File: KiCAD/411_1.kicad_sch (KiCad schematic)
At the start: 89 parts, among them J1 Conn_Coaxial, J2 Conn_Coaxial, J3 Conn_Coaxial, J4 Conn_01x05, SW1 SW_Push, U1 LM2937IMP, U2 MCP6L04x-xSL, U3 TMUX1101, U4 LA72914V-TLM-H, U5 ATtiny85V-10S

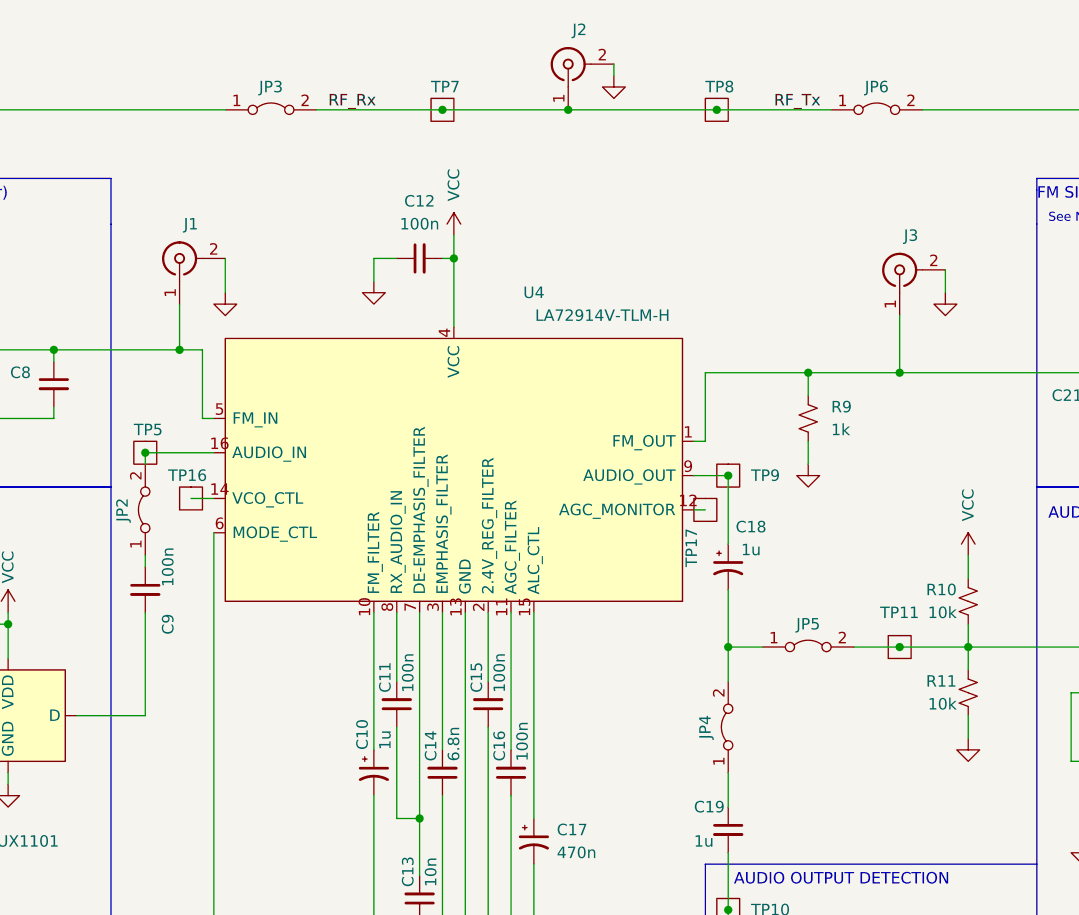
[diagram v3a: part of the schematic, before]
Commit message: Added info to components for bom generation
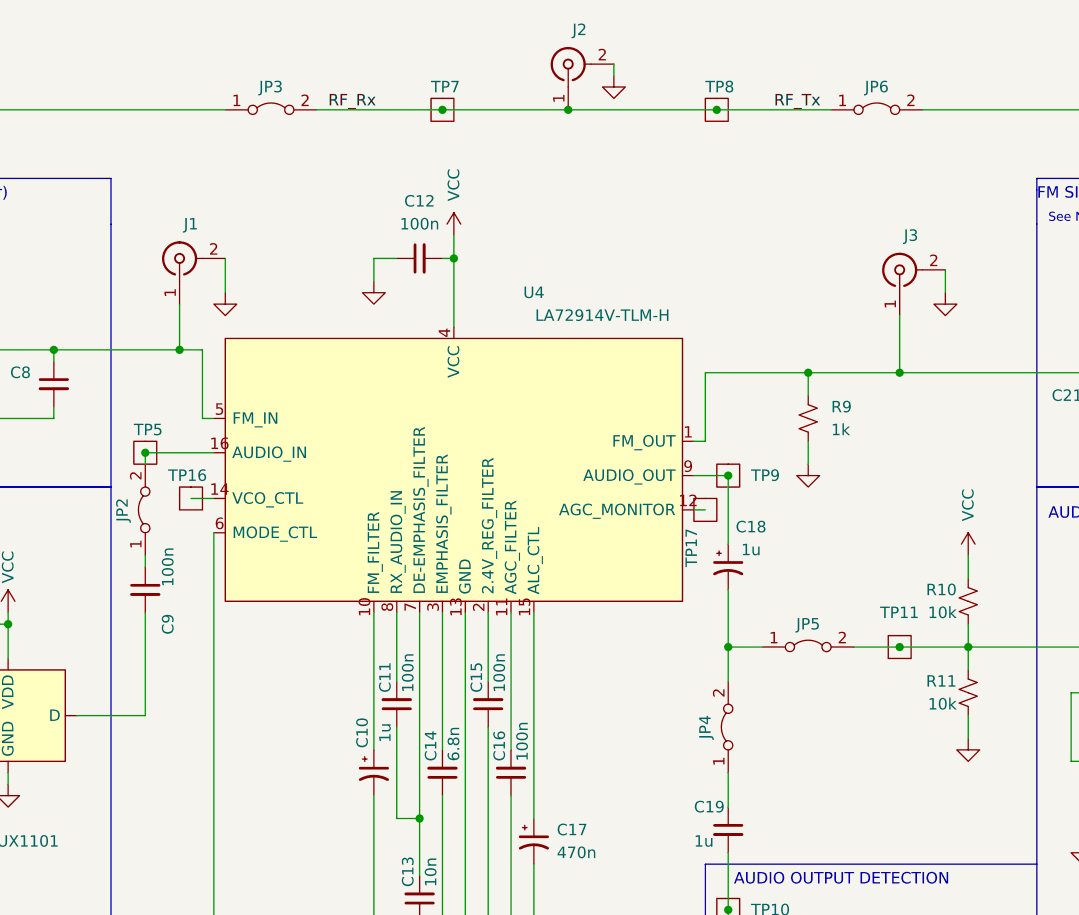
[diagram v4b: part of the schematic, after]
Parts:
- C10, C18: Cost Ea (none) -> .1; DPN (none) -> 732-8851-1-ND; Distributor (none) -> Digi-Key; MPN (none) -> 860020672005
- C17: Cost Ea (none) -> .11; DPN (none) -> 732-8656-1-ND; Distributor (none) -> Digi-Key; MPN (none) -> 860010672004
- J1, J3: Cost Ea (none) -> .77; DPN (none) -> WM5587TR-ND; Distributor (none) -> Digi-Key; MPN (none) -> 0734120110
- J2: Cost Ea (none) -> 5.27; DPN (none) -> ACX1230-ND; Distributor (none) -> Digi-Key; MPN (none) -> 132134
- U1: Cost Ea (none) -> 3.25; DPN (none) -> LM2937IMP-5.0TR-ND; Distributor (none) -> Digi-Key; MPN (none) -> LM2937IMP-5.0
- U3: Cost Ea (none) -> .51; DPN (none) -> 1727-4014-2-ND; Distributor (none) -> Digi-Key; MPN (none) -> 74HC4053PW,118
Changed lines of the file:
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@@
     (pin "2")
   )
-  (symbol (lib_name "C_Polarized_Small_US_2") (lib_id "Device:C_Polarized_Small_US") (at 138.43 96.52 0) (unit 1)
-    (in_bom yes) (on_board yes)
-    (property "Reference" "C10" (id 0) (at 137.16 93.98 90)
-      (effects (font (size 1.27 1.27)) (justify left))
-    )
-    (property "Value" "1u" (id 1) (at 139.7 93.98 90)
-      (effects (font (size 1.27 1.27)) (justify left))
-    )
+  (symbol (lib_name "C_Polarized_Small_US_1") (lib_id "Device:C_Polarized_Small_US") (at 138.43 96.52 0) (unit 1)
+    (in_bom yes) (on_board yes)
+    (property "Reference" "C10" (id 0) (at 137.16 92.075 90))
+    (property "Value" "1u" (id 1) (at 139.7 92.075 90))
     (property "Footprint" "Capacitor_THT:C_Radial_D5.0mm_H5.0mm_P2.00mm" (id 2) (at 138.43 96.52 0)
       (effects (font (size 1.27 1.27)) hide)
     )
     (property "Datasheet" "~" (id 3) (at 138.43 96.52 0)
+      (effects (font (size 1.27 1.27)) hide)
+    )
+    (property "Cost Ea" ".1" (id 4) (at 138.43 96.52 0)
+      (effects (font (size 1.27 1.27)) hide)
+    )
+    (property "DPN" "732-8851-1-ND" (id 5) (at 138.43 96.52 0)
+      (effects (font (size 1.27 1.27)) hide)
+    )
+    (property "Description" "1 µF 50 V Aluminum Electrolytic Capacitors Radial" (id 6) (at 138.43 96.52 0)
+      (effects (font (size 1.27 1.27)) hide)
+    )
+    (property "Distributor" "Digi-Key" (id 7) (at 138.43 96.52 0)
+      (effects (font (size 1.27 1.27)) hide)
+    )
+    (property "MPN" "860020672005" (id 8) (at 138.43 96.52 0)
       (effects (font (size 1.27 1.27)) hide)
     )
@@
       (effects (font (size 1.27 1.27)) hide)
     )
+    (property "Cost Ea" ".11" (id 4) (at 156.21 104.14 0)
+      (effects (font (size 1.27 1.27)) hide)
+    )
+    (property "DPN" "732-8656-1-ND" (id 5) (at 156.21 104.14 0)
+      (effects (font (size 1.27 1.27)) hide)
+    )
+    (property "Description" "0.47 µF 50 V Aluminum Electrolytic Capacitors Radial" (id 6) (at 156.21 104.14 0)
+      (effects (font (size 1.27 1.27)) hide)
+    )
+    (property "Distributor" "Digi-Key" (id 7) (at 156.21 104.14 0)
+      (effects (font (size 1.27 1.27)) hide)
+    )
+    (property "MPN" "860010672004" (id 8) (at 156.21 104.14 0)
+      (effects (font (size 1.27 1.27)) hide)
+    )
     (pin "1")
     (pin "2")
@@
     )
     (property "Datasheet" "~" (id 3) (at 177.8 73.66 0)
+      (effects (font (size 1.27 1.27)) hide)
+    )
+    (property "Cost Ea" ".1" (id 4) (at 177.8 73.66 0)
+      (effects (font (size 1.27 1.27)) hide)
+    )
+    (property "DPN" "732-8851-1-ND" (id 5) (at 177.8 73.66 0)
+      (effects (font (size 1.27 1.27)) hide)
+    )
+    (property "Description" "1 µF 50 V Aluminum Electrolytic Capacitors Radial" (id 6) (at 177.8 73.66 0)
+      (effects (font (size 1.27 1.27)) hide)
+    )
+    (property "Distributor" "Digi-Key" (id 7) (at 177.8 73.66 0)
+      (effects (font (size 1.27 1.27)) hide)
+    )
+    (property "MPN" "860020672005" (id 8) (at 177.8 73.66 0)
       (effects (font (size 1.27 1.27)) hide)
     )
@@
       (effects (font (size 1.27 1.27)) hide)
     )
+    (property "Cost Ea" ".77" (id 4) (at 116.84 39.37 90)
+      (effects (font (size 1.27 1.27)) hide)
+    )
+    (property "DPN" "WM5587TR-ND" (id 5) (at 116.84 39.37 90)
+      (effects (font (size 1.27 1.27)) hide)
+    )
+    (property "Description" "CONN UMC RCPT STR 50 OHM SMD" (id 6) (at 116.84 39.37 90)
+      (effects (font (size 1.27 1.27)) hide)
+    )
+    (property "Distributor" "Digi-Key" (id 7) (at 116.84 39.37 90)
+      (effects (font (size 1.27 1.27)) hide)
+    )
+    (property "MPN" "0734120110" (id 8) (at 116.84 39.37 90)
+      (effects (font (size 1.27 1.27)) hide)
+    )
     (pin "1")
     (pin "2")
@@
       (effects (font (size 1.27 1.27)) hide)
     )
+    (property "Cost Ea" "5.27" (id 4) (at 160.02 17.78 90)
+      (effects (font (size 1.27 1.27)) hide)
+    )
+    (property "DPN" "ACX1230-ND" (id 5) (at 160.02 17.78 90)
+      (effects (font (size 1.27 1.27)) hide)
+    )
+    (property "Description" "CONN SMA JACK STR 50 OHM PCB" (id 6) (at 160.02 17.78 90)
+      (effects (font (size 1.27 1.27)) hide)
+    )
+    (property "Distributor" "Digi-Key" (id 7) (at 160.02 17.78 90)
+      (effects (font (size 1.27 1.27)) hide)
+    )
+    (property "MPN" "132134" (id 8) (at 160.02 17.78 90)
+      (effects (font (size 1.27 1.27)) hide)
+    )
     (pin "1")
     (pin "2")
@@
     )
     (property "Datasheet" " ~" (id 3) (at 196.85 40.64 0)
+      (effects (font (size 1.27 1.27)) hide)
+    )
+    (property "Cost Ea" ".77" (id 4) (at 196.85 40.64 90)
+      (effects (font (size 1.27 1.27)) hide)
+    )
+    (property "DPN" "WM5587TR-ND" (id 5) (at 196.85 40.64 90)
+      (effects (font (size 1.27 1.27)) hide)
+    )
+    (property "Description" "CONN UMC RCPT STR 50 OHM SMD" (id 6) (at 196.85 40.64 90)
+      (effects (font (size 1.27 1.27)) hide)
+    )
+    (property "Distributor" "Digi-Key" (id 7) (at 196.85 40.64 90)
+      (effects (font (size 1.27 1.27)) hide)
+    )
+    (property "MPN" "0734120110" (id 8) (at 196.85 40.64 90)
       (effects (font (size 1.27 1.27)) hide)
     )
@@
       (effects (font (size 1.27 1.27)) hide)
     )
+    (property "Cost Ea" "3.25" (id 4) (at 49.53 135.89 0)
+      (effects (font (size 1.27 1.27)) hide)
+    )
+    (property "DPN" "LM2937IMP-5.0TR-ND" (id 5) (at 49.53 135.89 0)
+      (effects (font (size 1.27 1.27)) hide)
+    )
+    (property "Description" "Linear Voltage Regulator IC Positive Fixed 1 Output 400mA" (id 6) (at 49.53 135.89 0)
+      (effects (font (size 1.27 1.27)) hide)
+    )
+    (property "Distributor" "Digi-Key" (id 7) (at 49.53 135.89 0)
+      (effects (font (size 1.27 1.27)) hide)
+    )
+    (property "MPN" "LM2937IMP-5.0" (id 8) (at 49.53 135.89 0)
+      (effects (font (size 1.27 1.27)) hide)
+    )
     (pin "1")
     (pin "2")
@@
     )
     (property "Datasheet" "" (id 3) (at 95.25 99.06 0)
+      (effects (font (size 1.27 1.27)) hide)
+    )
+    (property "Cost Ea" ".51" (id 4) (at 97.79 90.17 0)
+      (effects (font (size 1.27 1.27)) hide)
+    )
+    (property "DPN" "1727-4014-2-ND" (id 5) (at 97.79 90.17 0)
+      (effects (font (size 1.27 1.27)) hide)
+    )
+    (property "Description" "IC MUX/DEMUX TRIPLE 2X1" (id 6) (at 97.79 90.17 0)
+      (effects (font (size 1.27 1.27)) hide)
+    )
+    (property "Distributor" "Digi-Key" (id 7) (at 97.79 90.17 0)
+      (effects (font (size 1.27 1.27)) hide)
+    )
+    (property "MPN" "74HC4053PW,118" (id 8) (at 97.79 90.17 0)
       (effects (font (size 1.27 1.27)) hide)
     )
@@
       (reference "C9") (unit 1) (value "100n") (footprint "Capacitor_SMD:C_0603_1608Metric_Pad1.08x0.95mm_HandSolder")
     )
-    (path "/6092f2a4-38e0-4a35-8135-fbb19041ddd0"
+    (path "/572aeab1-710b-4406-90fa-d7f8f8d407ef"
       (reference "C10") (unit 1) (value "1u") (footprint "Capacitor_THT:C_Radial_D5.0mm_H5.0mm_P2.00mm")
     )
@@
       (reference "J2") (unit 1) (value "Conn_Coaxial") (footprint "Connector_Coaxial:SMA_Amphenol_132134_Vertical")
     )
-    (path "/a4b43118-98fe-4b29-a04f-4f5b7ae18a55"
+    (path "/52790734-d415-40e7-9351-d9f500f1413c"
       (reference "J3") (unit 1) (value "Conn_Coaxial") (footprint "Connector_Coaxial:U.FL_Molex_MCRF_73412-0110_Vertical")
     )

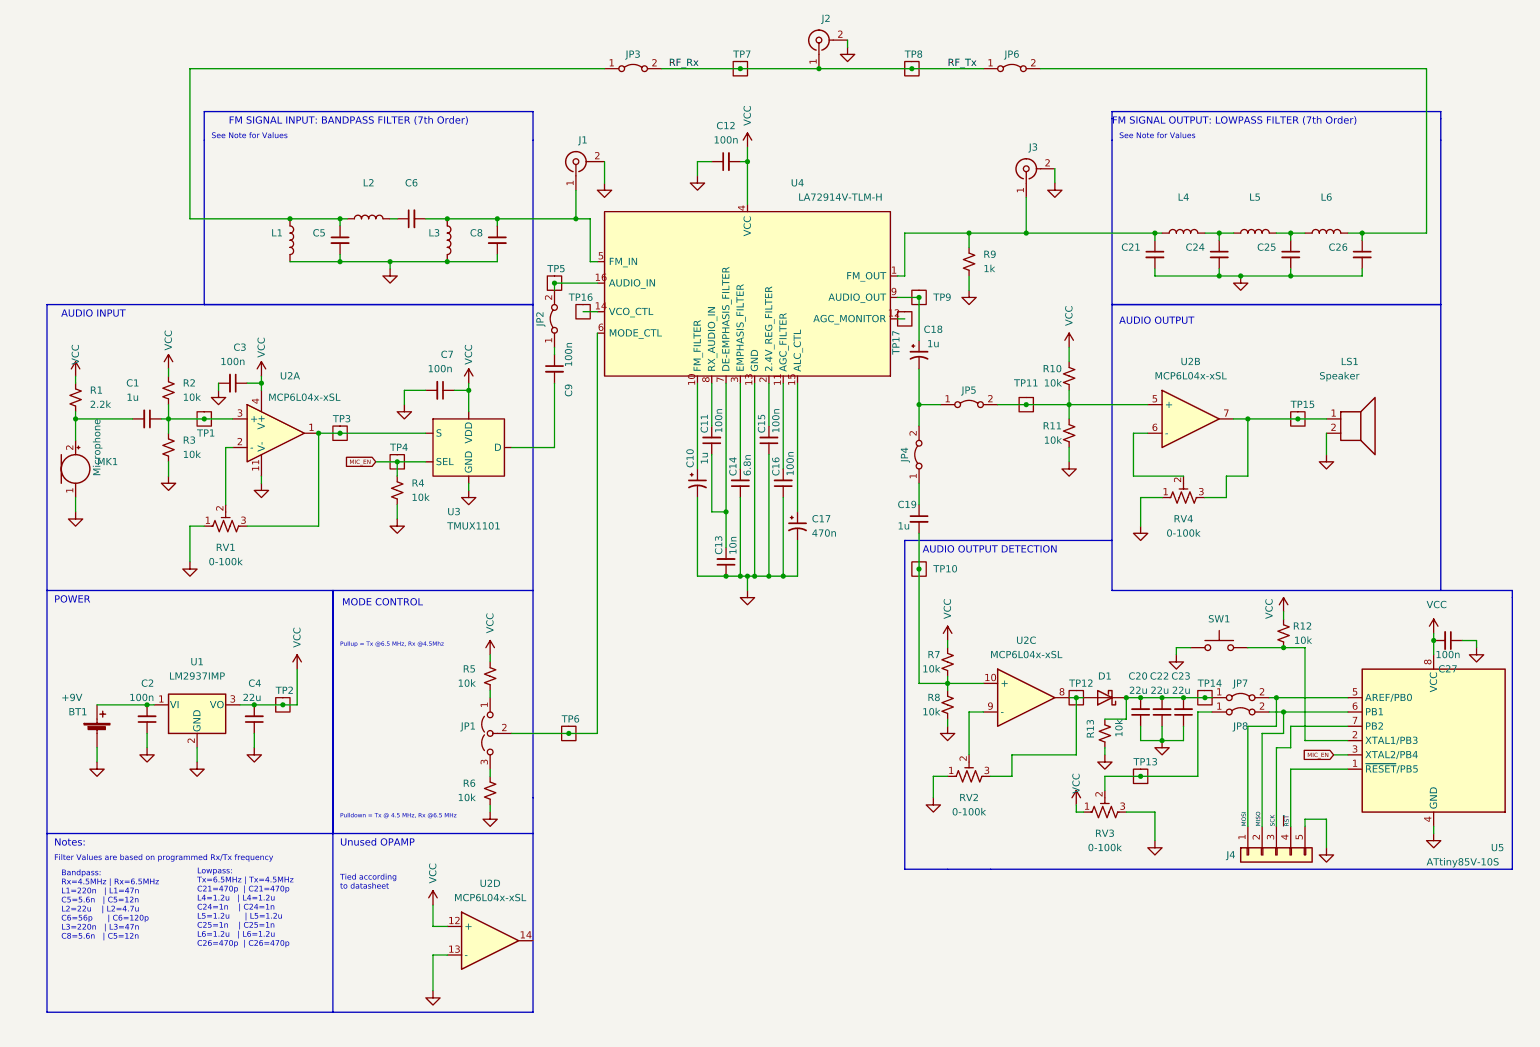
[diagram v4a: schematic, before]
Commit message: Fixed look up values for filter values
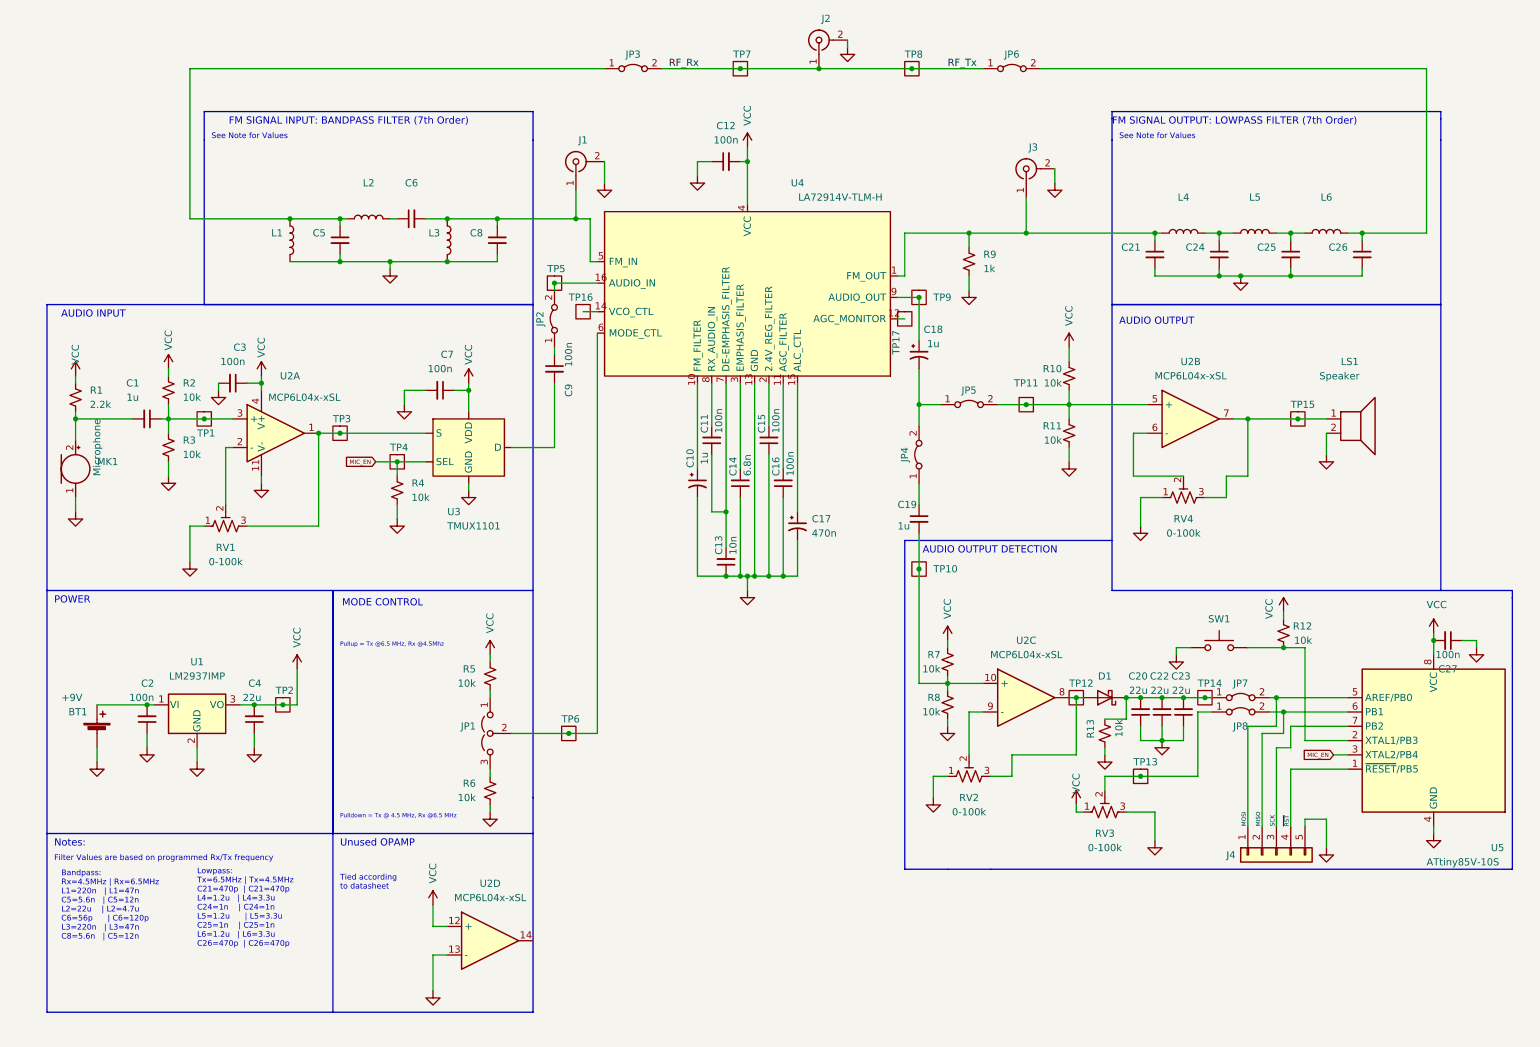
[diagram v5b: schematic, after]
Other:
- note added: "Lowpass: Tx=6.5MHz | Tx=4.5MHz C21=470p | C21=470p L4=1.2u | L4=3.3u C24=1n | C24=1n L5=1.2u | L5=3.3u C25=1n | C25=1n L6=1.2u | L6=3.3u C26=470p | C26=470p"
- note removed: "Lowpass: Tx=6.5MHz | Tx=4.5MHz C21=470p | C21=470p L4=1.2u | L4=1.2u C24=1n | C24=1n L5=1.2u | L5=1.2u C25=1n | C25=1n L6=1.2u | L6=1.2u C26=470p | C26=470p"
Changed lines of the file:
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@@
     (effects (font (size 1.27 1.27)) (justify right bottom))
   )
-  (text "Lowpass:\nTx=6.5MHz | Tx=4.5MHz\nC21=470p  | C21=470p\nL4=1.2u   | L4=1.2u\nC24=1n    | C24=1n\nL5=1.2u	  | L5=1.2u\nC25=1n    | C25=1n\nL6=1.2u   | L6=1.2u\nC26=470p  | C26=470p"
+  (text "Lowpass:\nTx=6.5MHz | Tx=4.5MHz\nC21=470p  | C21=470p\nL4=1.2u   | L4=3.3u\nC24=1n    | C24=1n\nL5=1.2u	  | L5=3.3u\nC25=1n    | C25=1n\nL6=1.2u   | L6=3.3u\nC26=470p  | C26=470p"
     (at 49.53 179.07 0)
     (effects (font (size 1 1)) (justify left bottom))
